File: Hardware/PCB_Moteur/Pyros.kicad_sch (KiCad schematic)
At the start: 33 parts, among them J17 Screw_Terminal_01x04, Q1 SI5442DU-T1-GE3, Q2 SI5442DU-T1-GE3, Q3 MMBT3904, Q4 SI7617DN-T1-GE3, U6 LM393

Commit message: wip: layout circuits Pyro
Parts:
- R36, R37, R38, R39, R40, R41, R42, R43, R44, R45, R46, R47, R48, R51, R52: footprint Resistor_SMD:R_0603_1608Metric -> Resistor_SMD:R_0805_2012Metric
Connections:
- net Pyro1-: now also J17.4 (Pin_4); no longer J17.2 (Pin_2)
- net Pyro2-: now also J17.1 (Pin_1); no longer J17.4 (Pin_4)
- net Vin_Pyro: now also J17.2 (Pin_2); no longer J17.1 (Pin_1)
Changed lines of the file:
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@@
 	(wire
 		(pts
+			(xy 171.45 100.33) (xy 175.26 100.33)
+		)
+		(stroke
+			(width 0)
+			(type default)
+		)
+	)
+	(wire
+		(pts
 			(xy 128.27 86.36) (xy 115.57 86.36)
 		)
@@
 	(wire
 		(pts
-			(xy 171.45 97.79) (xy 175.26 97.79)
-		)
-		(stroke
-			(width 0)
-			(type default)
-		)
-	)
-	(wire
-		(pts
 			(xy 134.62 100.33) (xy 134.62 101.6)
 		)
@@
 	(wire
 		(pts
-			(xy 171.45 100.33) (xy 175.26 100.33)
-		)
-		(stroke
-			(width 0)
-			(type default)
-		)
-	)
-	(wire
-		(pts
 			(xy 26.67 43.18) (xy 26.67 48.26)
 		)
@@
 	(wire
 		(pts
+			(xy 171.45 97.79) (xy 175.26 97.79)
+		)
+		(stroke
+			(width 0)
+			(type default)
+		)
+	)
+	(wire
+		(pts
 			(xy 223.52 27.94) (xy 223.52 33.02)
 		)
@@
 	(global_label "Vin_Pyro"
 		(shape input)
-		(at 171.45 97.79 180)
+		(at 171.45 100.33 180)
 		(fields_autoplaced yes)
 		(effects
@@
 		)
 		(property "Intersheetrefs" "${INTERSHEET_REFS}"
-			(at 160.482 97.79 0)
+			(at 160.482 100.33 0)
 			(effects
 				(font
@@
 		)
 	)
-	(global_label "Cmp_2"
+	(global_label "Pyro2-"
 		(shape input)
-		(at 67.31 50.8 0)
+		(at 171.45 97.79 180)
 		(fields_autoplaced yes)
 		(effects
@@
 				(size 1.27 1.27)
 			)
-			(justify left)
+			(justify right)
 		)
 		(property "Intersheetrefs" "${INTERSHEET_REFS}"
-			(at 76.5846 50.8 0)
+			(at 161.5101 97.79 0)
 			(effects
 				(font
 					(size 1.27 1.27)
 				)
-				(justify left)
+				(justify right)
 				(hide yes)
 			)
@@
 	(global_label "Cmp_2"
 		(shape input)
-		(at 92.71 109.22 180)
+		(at 67.31 50.8 0)
 		(fields_autoplaced yes)
 		(effects
@@
 				(size 1.27 1.27)
 			)
-			(justify right)
+			(justify left)
 		)
 		(property "Intersheetrefs" "${INTERSHEET_REFS}"
-			(at 83.4354 109.22 0)
+			(at 76.5846 50.8 0)
 			(effects
 				(font
 					(size 1.27 1.27)
 				)
-				(justify right)
+				(justify left)
 				(hide yes)
 			)
 		)
 	)
-	(global_label "PA_An"
+	(global_label "Cmp_2"
 		(shape input)
-		(at 240.03 62.23 180)
+		(at 92.71 109.22 180)
 		(fields_autoplaced yes)
 		(effects
@@
 		)
 		(property "Intersheetrefs" "${INTERSHEET_REFS}"
-			(at 231.481 62.23 0)
+			(at 83.4354 109.22 0)
 			(effects
 				(font
@@
 		)
 	)
-	(global_label "Vin_Pyro"
+	(global_label "PA_An"
 		(shape input)
-		(at 44.45 86.36 180)
+		(at 240.03 62.23 180)
 		(fields_autoplaced yes)
 		(effects
@@
 		)
 		(property "Intersheetrefs" "${INTERSHEET_REFS}"
-			(at 33.482 86.36 0)
+			(at 231.481 62.23 0)
 			(effects
 				(font
@@
 		)
 	)
-	(global_label "Pyro1-"
+	(global_label "Vin_Pyro"
 		(shape input)
-		(at 171.45 100.33 180)
+		(at 44.45 86.36 180)
 		(fields_autoplaced yes)
 		(effects
@@
 		)
 		(property "Intersheetrefs" "${INTERSHEET_REFS}"
-			(at 161.5101 100.33 0)
+			(at 33.482 86.36 0)
 			(effects
 				(font
@@
 		)
 	)
-	(global_label "Vin_Pyro"
+	(global_label "Pyro1-"
 		(shape input)
-		(at 115.57 95.25 0)
+		(at 171.45 105.41 180)
 		(fields_autoplaced yes)
 		(effects
@@
 				(size 1.27 1.27)
 			)
-			(justify left)
+			(justify right)
 		)
 		(property "Intersheetrefs" "${INTERSHEET_REFS}"
-			(at 126.538 95.25 0)
+			(at 161.5101 105.41 0)
 			(effects
 				(font
 					(size 1.27 1.27)
 				)
-				(justify left)
+				(justify right)
 				(hide yes)
 			)
 		)
 	)
-	(global_label "Pyro2-"
+	(global_label "Vin_Pyro"
 		(shape input)
-		(at 171.45 105.41 180)
+		(at 115.57 95.25 0)
 		(fields_autoplaced yes)
 		(effects
@@
 				(size 1.27 1.27)
 			)
-			(justify right)
+			(justify left)
 		)
 		(property "Intersheetrefs" "${INTERSHEET_REFS}"
-			(at 161.5101 105.41 0)
+			(at 126.538 95.25 0)
 			(effects
 				(font
 					(size 1.27 1.27)
 				)
-				(justify right)
+				(justify left)
 				(hide yes)
 			)
@@
 			)
 		)
-		(property "Footprint" "Resistor_SMD:R_0603_1608Metric"
+		(property "Footprint" "Resistor_SMD:R_0805_2012Metric"
 			(at 31.75 58.42 0)
 			(effects
@@
 			)
 		)
-		(property "Footprint" "Resistor_SMD:R_0603_1608Metric"
+		(property "Footprint" "Resistor_SMD:R_0805_2012Metric"
 			(at 31.75 40.64 0)
 			(effects
@@
 			)
 		)
-		(property "Footprint" "Resistor_SMD:R_0603_1608Metric"
+		(property "Footprint" "Resistor_SMD:R_0805_2012Metric"
 			(at 52.07 101.6 0)
 			(effects
@@
 			)
 		)
-		(property "Footprint" "Resistor_SMD:R_0603_1608Metric"
+		(property "Footprint" "Resistor_SMD:R_0805_2012Metric"
 			(at 248.92 56.388 90)
 			(effects
@@
 			)
 		)
-		(property "Footprint" "Resistor_SMD:R_0603_1608Metric"
+		(property "Footprint" "Resistor_SMD:R_0805_2012Metric"
 			(at 59.69 109.22 0)
 			(effects
@@
 			)
 		)
-		(property "Footprint" "Resistor_SMD:R_0603_1608Metric"
+		(property "Footprint" "Resistor_SMD:R_0805_2012Metric"
 			(at 26.67 40.64 0)
 			(effects
@@
 			)
 		)
-		(property "Footprint" "Resistor_SMD:R_0603_1608Metric"
+		(property "Footprint" "Resistor_SMD:R_0805_2012Metric"
 			(at 101.6 115.57 0)
 			(effects
@@
 			)
 		)
-		(property "Footprint" "Resistor_SMD:R_0603_1608Metric"
+		(property "Footprint" "Resistor_SMD:R_0805_2012Metric"
 			(at 26.67 58.42 0)
 			(effects
@@
 			)
 		)
-		(property "Footprint" "Resistor_SMD:R_0603_1608Metric"
+		(property "Footprint" "Resistor_SMD:R_0805_2012Metric"
 			(at 120.65 101.6 0)
 			(effects
@@
 			)
 		)
-		(property "Footprint" "Resistor_SMD:R_0603_1608Metric"
+		(property "Footprint" "Resistor_SMD:R_0805_2012Metric"
 			(at 261.62 56.388 90)
 			(effects
@@
 			)
 		)
-		(property "Footprint" "Resistor_SMD:R_0603_1608Metric"
+		(property "Footprint" "Resistor_SMD:R_0805_2012Metric"
 			(at 27.94 119.38 0)
 			(effects
@@
 			)
 		)
-		(property "Footprint" "Resistor_SMD:R_0603_1608Metric"
+		(property "Footprint" "Resistor_SMD:R_0805_2012Metric"
 			(at 128.27 109.22 0)
 			(effects
@@
 			)
 		)
-		(property "Footprint" "Resistor_SMD:R_0603_1608Metric"
+		(property "Footprint" "Resistor_SMD:R_0805_2012Metric"
 			(at 96.52 119.38 0)
 			(effects
@@
 			)
 		)
-		(property "Footprint" "Resistor_SMD:R_0603_1608Metric"
+		(property "Footprint" "Resistor_SMD:R_0805_2012Metric"
 			(at 198.12 47.752 90)
 			(effects
@@
 			)
 		)
-		(property "Footprint" "Resistor_SMD:R_0603_1608Metric"
+		(property "Footprint" "Resistor_SMD:R_0805_2012Metric"
 			(at 33.02 115.57 0)
 			(effects

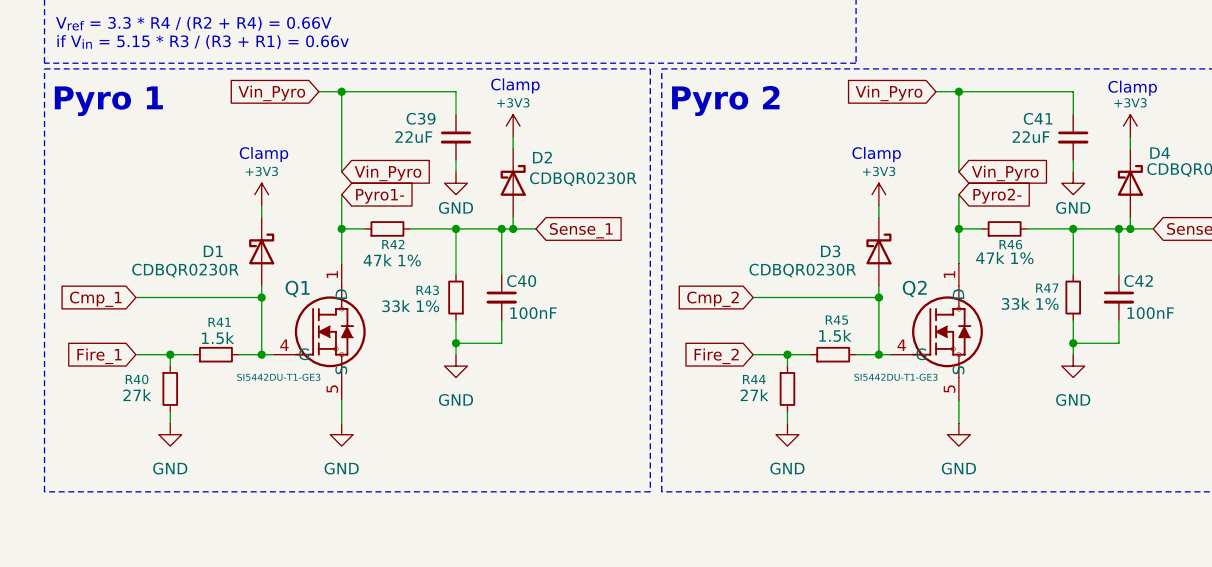
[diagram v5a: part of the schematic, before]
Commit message: wip: finit routing servo et limit switch, début pyro
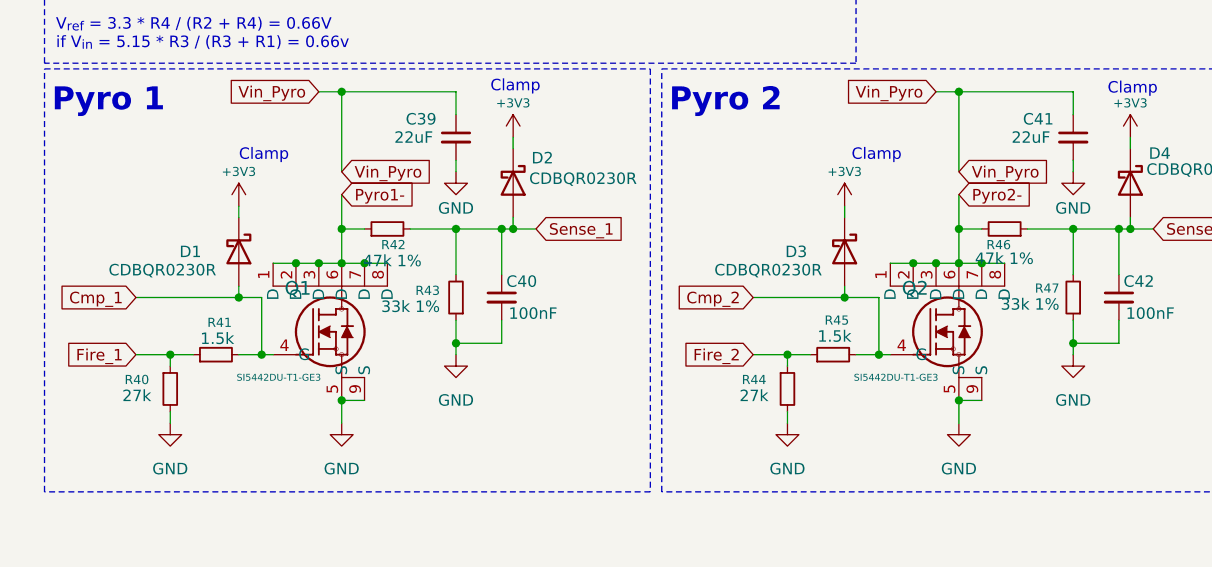
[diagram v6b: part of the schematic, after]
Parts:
- Q1, Q2: footprint pcb_moteur:SI5442DU_T1_G3 -> SON_8DU-T1-GE3_VIS
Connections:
- net GND: now also Q1.9 (S), Q2.9 (S)
- net Pyro1-: now also Q1.2 (D), Q1.3 (D), Q1.6 (D), Q1.7 (D), Q1.8 (D)
- net Pyro2-: now also Q2.2 (D), Q2.3 (D), Q2.6 (D), Q2.7 (D), Q2.8 (D), R46.2; no longer R46.1
- net Sense_2: now also R46.1; no longer R46.2
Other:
- moved on the sheet: D1, D3, R46

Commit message: wip: pyro suite
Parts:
- Q1, Q2: footprint SON_8DU-T1-GE3_VIS -> pcb_moteur:SI5442DU_T1_G3
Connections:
- net GND: no longer Q1.9 (S), Q2.9 (S)
- net Pyro1-: no longer Q1.2 (D), Q1.3 (D), Q1.6 (D), Q1.7 (D), Q1.8 (D)
- net Pyro2-: no longer Q2.2 (D), Q2.3 (D), Q2.6 (D), Q2.7 (D), Q2.8 (D)
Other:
- moved on the sheet: D1, D3
